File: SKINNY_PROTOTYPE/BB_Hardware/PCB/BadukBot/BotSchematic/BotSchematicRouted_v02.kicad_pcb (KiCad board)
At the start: 2 copper layers, 93 x 22.5 mm, 90 parts, among them J1 MOLEX781710002, J10 A316DA2SV71, J11 62401621722, J12 A316DA2SV71, J13 0877601616, J2 MOLEX781710003, M1 Pos1a, M2 Neg1a, M3 Pos2a, M4 Neg2a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

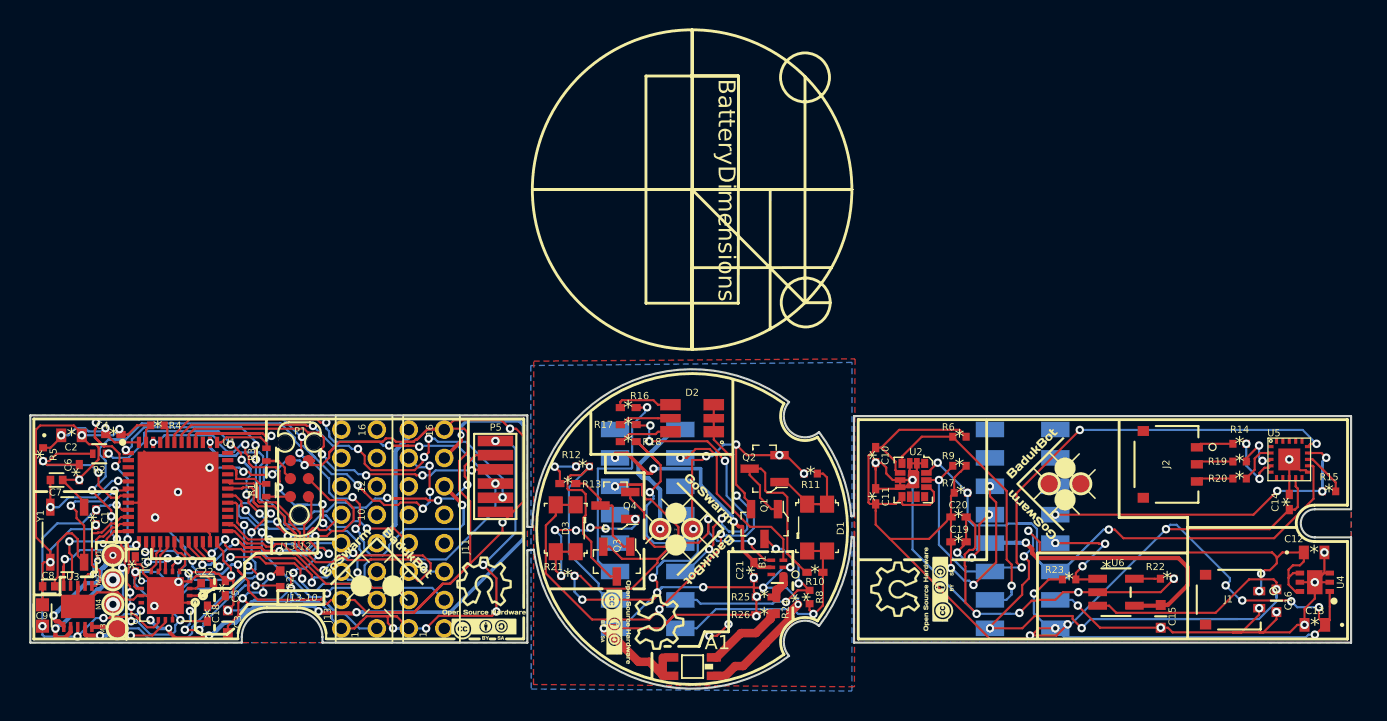
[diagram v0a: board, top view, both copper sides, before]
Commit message: Changed PCB for more compact component placement, shortened board 3, added images for the new layout
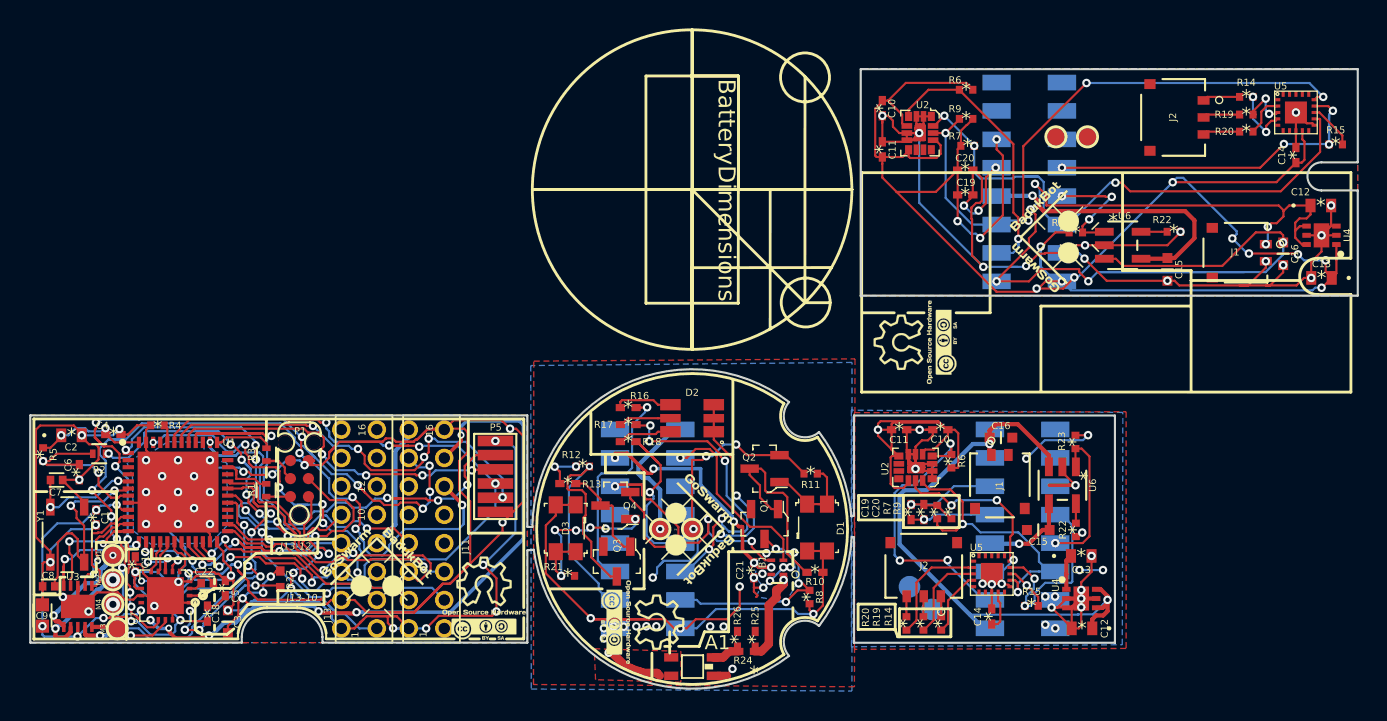
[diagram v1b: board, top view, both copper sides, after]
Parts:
- removed G6: LOGO, Silk:links_20mm
- removed the TESTPOINT-50MIL at (143.7, 104.6)
- removed the TESTPOINT-50MIL at (141.4, 104.6)
- added C10: 100nF, 100nf:C0402C104K4RACTU, F.Cu at (129.7, 78.1)
- added C11: 100nF, 100nf:C0402C104K4RACTU, F.Cu at (129.7, 81.0)
- added C12: 1uF, 1uF:0603ZD105KAT2A, F.Cu at (160.5, 85.0)
- added C13: 1uF, 1uF:0603ZD105KAT2A, F.Cu at (160.6, 90.1)
- added C14: 100nF, 100nf:C0402C104K4RACTU, F.Cu at (158.8, 81.4)
- added C15: TAIYO_YUDEN_LMK107BJ475KA-T, TAIYO_YUDEN_LMK107BJ475KA-T:TAIYO_YUDEN_LMK107BJ475KA-T_0, F.Cu at (149.7, 89.5)
- added C16: Taiyo, TAIYO_YUDEN_LMK107BJ475KA-T:TAIYO_YUDEN_LMK107BJ475KA-T_0, F.Cu at (157.9, 88.4)
- added C19: 10nF, 100nf:C0402C104K4RACTU, F.Cu at (135.5, 84.2)
- added C20: 1nF, 100nf:C0402C104K4RACTU, F.Cu at (135.5, 82.5)
- added G***: LOGO, Silk:links, B.Cu at (144.3, 107.7)
- added G10: LOGO, Silk:OpenHardwareLogo, B.Cu at (131.7, 103.6)
- added G11: LOGO, Silk:BadukBot-GoSwarm, B.Cu at (131.8, 112.0)
- added J1: MOLEX781710002, MOLEX_78171-0002:MOLEX_78171-0002_0, F.Cu at (154.5, 88.3)
- added J12: A316DA2SV71, A13:A13_1, B.Cu at (140.6, 83.3)
- added J2: MOLEX781710003, MOLEX_78171-0003:MOLEX_78171-0003_0, F.Cu at (150.1, 78.8)
- added P4: Conn_01x02_Female, Connector_DIN:Conn_01x02_Female, B.Cu at (132.4, 112.6)
- added R14: 10K, 10K0402:CRCW040210K0FKED, F.Cu at (155.3, 77.3)
- added R15: 100K, 100K:CRCW0402100KFKED, F.Cu at (161.6, 80.7)
- added R19: 10K, 10K0402:CRCW040210K0FKED, F.Cu at (155.3, 78.6)
- added R20: 10K, 10K0402:CRCW040210K0FKED, F.Cu at (155.3, 79.8)
- added R22: 10K, 10K0402:CRCW040210K0FKED, F.Cu at (150.2, 86.8)
- added R23: 100K, 100K:CRCW0402100KFKED, F.Cu at (143.3, 86.9)
- added R6: 100K, 100K:CRCW0402100KFKED, F.Cu at (135.6, 76.8)
- added R7: 10K, 10K0402:CRCW040210K0FKED, F.Cu at (135.7, 80.8)
- added R9: 10K, 10K0402:CRCW040210K0FKED, F.Cu at (135.6, 78.9)
- added TESTPOINT-50MIL: VAL**, gsg-modules:TESTPOINT-50MIL, F.Cu at (141.9, 80.1)
- added TESTPOINT-50MIL: VAL**, gsg-modules:TESTPOINT-50MIL, F.Cu at (144.1, 80.1)
- added U2: LSM6DS3, digikey-footprints:LGA-14L_2.5x3mm__LSM6DS3, F.Cu at (132.3, 79.9)
- added U4: ADP122ACPZ33R7, ADP122ACPZ-3.3-R7:SON65P200X200X60-7N-D, F.Cu at (160.6, 87.1)
- added U5: AT42QT1070MMHCTND, vq:VQFN_20PAD, F.Cu at (158.8, 78.4)
- added U6: MCP73831T2ACIOT, MCP:MCP73831T-2ACI&slash_OT, F.Cu at (146.6, 87.8)
- moved R20 25.6 mm to (131.4, 114.4), turned to 90 degrees
- moved R19 25.0 mm to (132.6, 114.4), turned to 90 degrees
- moved R14 24.5 mm to (133.8, 114.4), turned to 90 degrees
- moved C16 22.5 mm to (138.0, 101.3), turned to 0 degrees
- moved C14 22.4 mm to (137.4, 113.9)
- moved R15 22.4 mm to (140.2, 113.2)
- moved U5 22.4 mm to (137.4, 110.9)
- moved J2 18.5 mm to (132.6, 110.3), turned to 180 degrees
- moved J1 18.0 mm to (138.0, 104.7), turned to 0 degrees
- moved G1 17.4 mm to (141.9, 87.2)
- moved G2 17.4 mm to (132.0, 94.6)
- moved C12 17.2 mm to (143.7, 114.8), turned to 180 degrees
- moved C13 17.1 mm to (143.7, 109.7), turned to 0 degrees
- moved U4 16.5 mm to (143.7, 112.7), turned to 0 degrees
- moved C15 10.6 mm to (140.7, 107.8), turned to 180 degrees
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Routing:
- net 23aGround: track 73.4 -> 123.9 mm, vias 15 -> 29
- net 2aGND: track 77.1 -> 26.7 mm, vias 18 -> 23
- net 21a33v: track 110.6 -> 158.4 mm, vias 11 -> 20
- net 22aVBAT: track 86.0 -> 129.7 mm, vias 7 -> 9
- net 25aSDA: track 42.1 -> 63.3 mm, vias 3 -> 5
- net 24aIMUINT: track 19.6 -> 40.0 mm, vias 1 -> 4
- net 2a_GND: track 30.4 -> 15.4 mm, vias 2 -> 1
- net ~29aTOUCHCHG~: track 26.1 -> 40.2 mm, vias 4 -> 6
- net 26aSCL: track 43.0 -> 57.1 mm, vias 4 -> 7
- net 27aCHARGING: track 9.40 -> 20.2 mm, vias 3 -> 4
- net Net-(R20-Pad1): track 2.95 -> 11.0 mm
- net 28aP41: track 21.3 -> 27.8 mm, vias 1 -> 2
- net Net-(R19-Pad1): track 3.52 -> 10.00 mm
- net Net-(B1-Pad1): track 1.84 -> 7.33 mm, vias 0 -> 1
- net Net-(R14-Pad1): track 4.28 -> 8.95 mm
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- added copper zone on B.Cu, net 2aGND
- added copper zone on B.Cu, net 2bGND
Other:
- board size 93 x 22.5 mm -> 93.5 x 43.6 mm

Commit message: Reduced board sizes, results in $6 saved per 3 boards at OSHPark
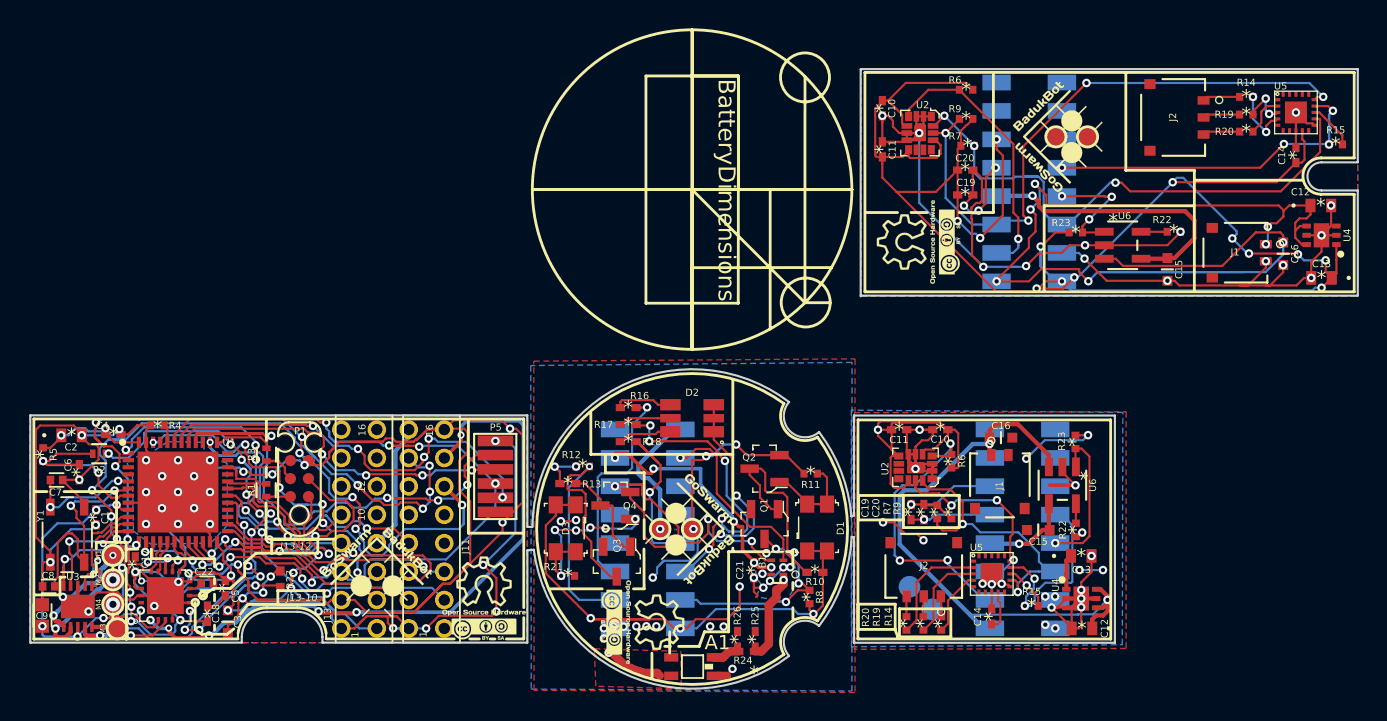
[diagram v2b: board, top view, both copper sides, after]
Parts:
- moved G2 7.06 mm to (132.2, 87.5)
- moved G1 7.06 mm to (142.1, 80.2)
- renumbered P4 to P10
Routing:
- net 23aGround: track 123.9 -> 127.2 mm, vias 29 -> 31
- net 4aPHOTODIODE2: track 22.8 -> 24.0 mm
- net 1a33v: track 62.0 -> 63.0 mm, vias 8 -> 10
